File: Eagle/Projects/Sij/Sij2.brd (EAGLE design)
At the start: 100 x 100 mm, 159 parts, among them M1 -30V

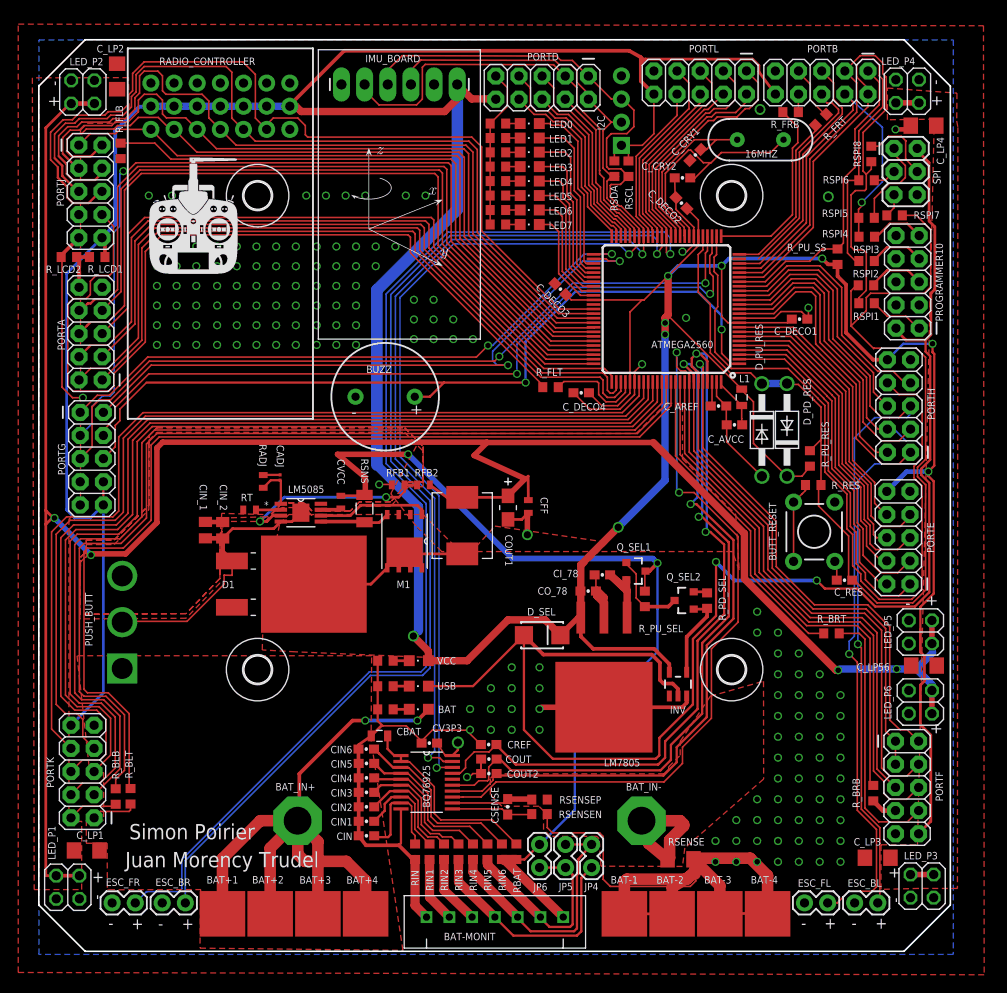
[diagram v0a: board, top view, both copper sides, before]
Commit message: Added code for I2C and IMU
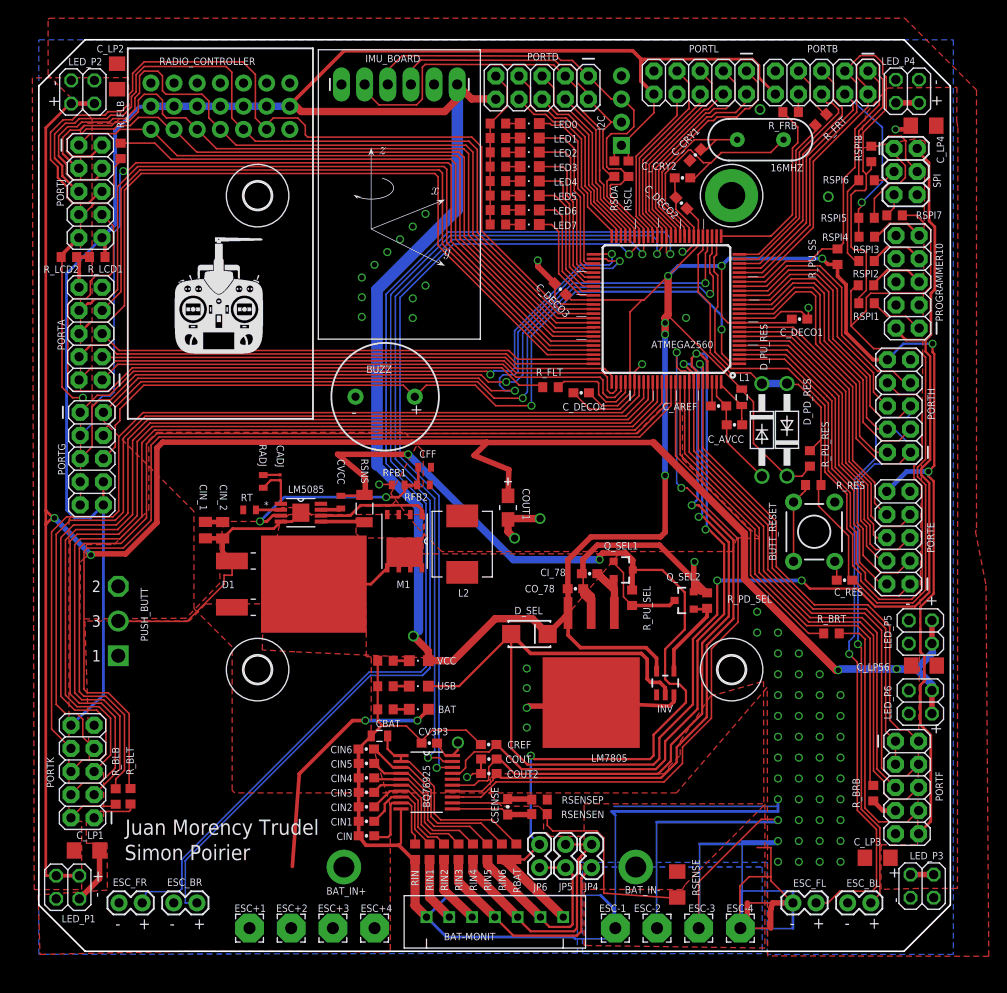
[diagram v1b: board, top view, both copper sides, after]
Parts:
- removed BAT+1, BAT+2, BAT+3, BAT+4, BAT-1, BAT-2, BAT-3, BAT-4: BULLET_PAD, custom_parts:4.5MM_SQUARE
- added ESC+1, ESC+2, ESC+3, ESC+4, ESC-1, ESC-2, ESC-3, ESC-4: WIREPAD3,17/1,3, wirepad:3,17/1,3
- H4: value MOUNT-HOLE3.0 -> MOUNT-PAD-ROUND3.0; device holes:3,0 -> holes:3,0-PAD
- Q_SEL1: value MOSFET-PCHANNEL -> DMN3099L
- Q_SEL2: value MOSFET-NCHANNELAO3404A -> DMN3023L
- moved CFF 12.2 mm to (42.3, 53.1), turned to 180 degrees
- moved BAT_IN+ 7.18 mm to (33.5, 9.24)
- moved BAT_IN- 5.12 mm to (65.5, 9.24)
- moved RSENSE 2.79 mm to (70.0, 7.33), turned to 90 degrees
- moved L2 2.03 mm to (46.5, 41.6)
- moved LM7805 1.49 mm to (60.6, 27.4)
- moved PUSH_BUTT 1.46 mm to (8.71, 32.4)
- moved CO_78 1.42 mm to (58.9, 39.8)
- moved INV 1.40 mm to (68.7, 29.4)
- moved Q_SEL1 1.40 mm to (64.1, 41.8)
- moved R_PU_SEL 1.40 mm to (65.1, 38.8)
- moved D_SEL 1.40 mm to (53.8, 34.8)
- moved CI_78 1.40 mm to (60.4, 41.4)
- moved ESC_BR 1.27 mm to (17.3, 5.31)
- moved ESC_FL 1.27 mm to (85.3, 5.31)
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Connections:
- net BAT+: now also ESC+1.1, ESC+2.1, ESC+3.1, ESC+4.1; no longer BAT+1.IN, BAT+2.IN, BAT+3.IN, BAT+4.IN
- net FB_5085: now also CFF.2
- net GND: now also ESC-1.1, ESC-2.1, ESC-3.1, ESC-4.1, H4.B3,0; no longer BAT-1.IN, BAT-2.IN, BAT-3.IN, BAT-4.IN, CFF.2
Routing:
- net GND: track 279.9 -> 496.1 mm, vias 163 -> 73
- net BAT+: track 81.4 -> 27.4 mm
- net LED_S_FLT: track 97.3 -> 77.5 mm
- net PA1: track 82.5 -> 63.1 mm
- net PA0: track 80.4 -> 61.3 mm
- net PA2: track 76.2 -> 57.5 mm
- net PA3: track 76.0 -> 57.8 mm
- net PA4: track 72.3 -> 55.3 mm
- net VOUT_5085: track 256.7 -> 240.1 mm
- net BAT-: track 14.6 -> 0.00 mm
- net V_BATT: track 106.6 -> 120.2 mm, vias 2 -> 3
- net LED_S_FLB: track 0.00 -> 9.14 mm
- net 9_5085: track 16.9 -> 8.79 mm
- net PG1: track 70.5 -> 74.0 mm
- net PG3: track 83.7 -> 87.1 mm
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- added copper zone on layer 1, net ISEN_5085
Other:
- board text added: "09/21/2016"
- board text added: "ESC+1"
- board text added: "ESC+2"
- board text added: "ESC+3"
- board text added: "ESC+4"
- board text added: "ESC-1"
- board text added: "ESC-2"
- board text added: "ESC-3"
- board text added: "ESC-4"
- board text added: "Power and uC interface board"
- board text added: "|"
- board text added: "© SiJ inc"
